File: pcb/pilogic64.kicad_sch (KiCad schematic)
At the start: 4 parts, among them U2 Pico

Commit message: More pcb!
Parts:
- added D1: D_Schottky, Diode_THT:D_DO-41_SOD81_P10.16mm_Horizontal, symbol Device:D_Schottky
- added SW1, SW2: RotaryEncoder_Switch, Rotary_Encoder:RotaryEncoder_Alps_EC11E-Switch_Vertical_H20mm, symbol Device:RotaryEncoder_Switch
- added b18650: ~, Battery:BatteryHolder_MPD_BH-18650-PC2, symbol LibrarySym:18650
- SD_SPI1: renamed from SD_SPI; footprint (none) -> Connector_PinHeader_2.54mm:PinHeader_1x06_P2.54mm_Vertical
- U2: footprint RPi_Pico:RPi_Pico_SMD_TH -> Library:RPi_Pico_SMD_TH
- renumbered MT3608_module_SMT to MT3608_module_SMT1
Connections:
- net at TP4056-18650.3 (OUT+): now also MT3608_module_SMT1.1 (VIN+)
- net at TP4056-18650.4 (OUT-): now also MT3608_module_SMT1.2 (VIN-)
- net at TP4056-18650.5 (B+): now also b18650.1 (+)
- net at TP4056-18650.6 (B-): now also b18650.2 (-)
- net GND: now reaches MT3608_module_SMT1.3 (VOUT-)
- net GND: now also SD_SPI1.6 (GND), U2.13 (GND), U2.18 (GND), U2.23 (GND), U2.28 (GND), U2.3 (GND), U2.38 (GND), U2.8 (GND), SW1.C, SW1.S2, SW2.C, SW2.S2
- net +5V: now reaches MT3608_module_SMT1.4 (VOUT+)
- net +5V: now also D1.2 (A)
- net +3.3V: now reaches SD_SPI1.1 (3.3V)
- net +3.3V: now also U2.36 (3V3), SW1.A, SW2.A
- net at SD_SPI1.2 (cs): now also U2.2 (GPIO1)
- net at SD_SPI1.3 (MOSI): now also U2.5 (GPIO3)
- net at SD_SPI1.4 (CLK): now also U2.4 (GPIO2)
- net at SD_SPI1.5 (MISO): now also U2.6 (GPIO4)
- net at U2.10 (GPIO7): now also SW2.S1
- net at U2.11 (GPIO8): now also SW1.B
- net at U2.12 (GPIO9): now also SW1.S1
- net at U2.39 (VSYS): now also D1.1 (K)
- net at U2.9 (GPIO6): now also SW2.B
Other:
- moved on the sheet: MT3608_module_SMT1, SD_SPI1, U2

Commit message: Finished cicuit, and I think also finished pcb
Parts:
- added U1: ~, Connector_PinHeader_2.54mm:PinHeader_1x04_P2.54mm_Vertical, symbol LibrarySym:I2C_OLED
- added U3: pam8403, Library:pam8403, symbol LibrarySym:pam8403
- b18650: footprint Battery:BatteryHolder_MPD_BH-18650-PC2 -> Library:18650-PC4
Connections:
- net +3.3V: now also U1.2 (VCC)
- net +5V: now also U3.4 (vin)
- net GND: now also U1.1 (GND), U3.2 (T), U3.5 (gnd)
- net at TP4056-18650.5 (B+): now also b18650.+1 (+), b18650.+2 (+); no longer b18650.1 (+)
- net at TP4056-18650.6 (B-): now also b18650.-1 (-), b18650.-2 (-); no longer b18650.2 (-)
- net at U2.14 (GPIO10): now also U1.4 (SDA)
- net at U2.15 (GPIO11): now also U1.3 (SCL)
- net at U2.19 (GPIO14): now also U3.3 (R)
- net at U2.20 (GPIO15): now also U3.1 (L)
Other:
- moved on the sheet: D1, MT3608_module_SMT1, SD_SPI1, TP4056-18650

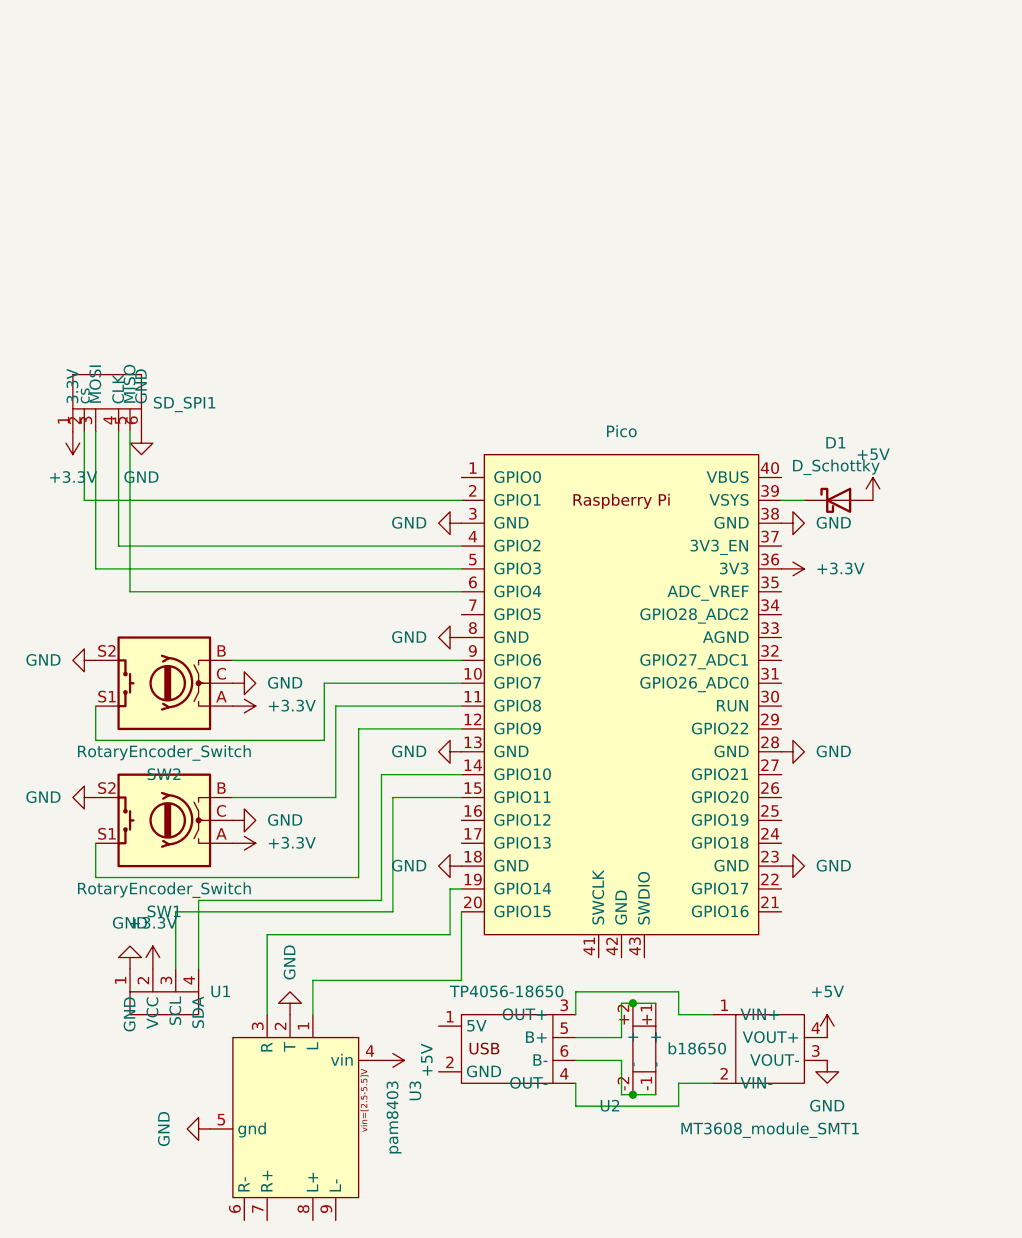
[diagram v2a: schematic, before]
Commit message: Add new symbols for components and remove lock files; implement main functionality for game selection on microcontroller
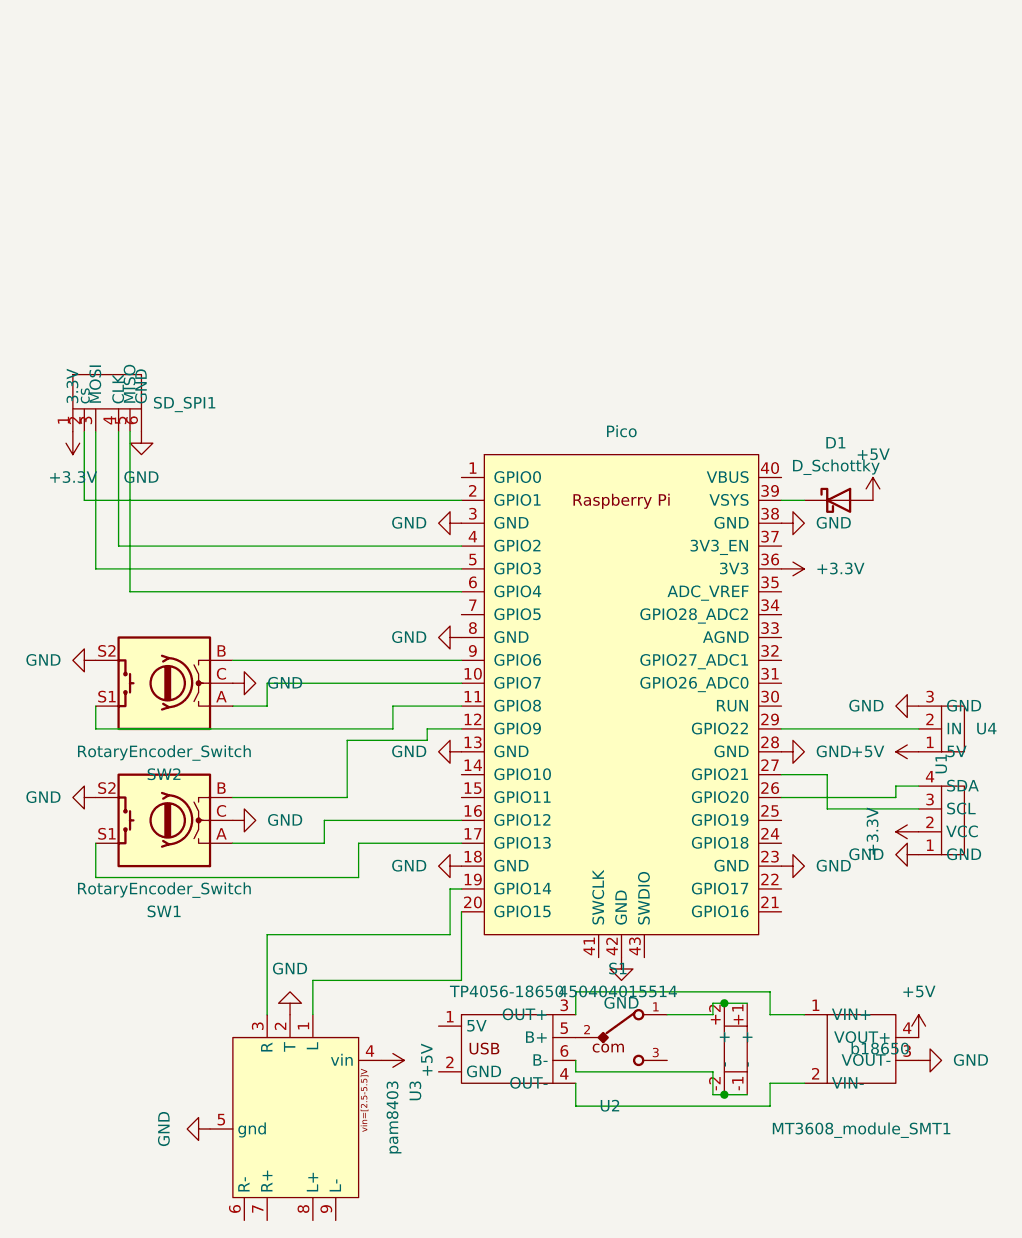
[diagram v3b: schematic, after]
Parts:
- added S1: 450404015514, Library:450404015514, symbol LibrarySym:450404015514
- added U4: ~, Library:8x8 MAtrix, symbol LibrarySym:8x8_matrix
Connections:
- net +3.3V: no longer SW1.A, SW2.A
- net +5V: now also U4.1 (5V)
- net GND: now also U2.42 (GND), U4.3 (GND)
- net at b18650.+1 (+), b18650.+2 (+): now also S1.1; no longer TP4056-18650.5 (B+)
- net at U2.10 (GPIO7): now also SW2.A; no longer SW2.S1
- net at U1.3 (SCL): now also U2.27 (GPIO21); no longer U2.15 (GPIO11)
- net at U1.4 (SDA): now also U2.26 (GPIO20); no longer U2.14 (GPIO10)
- net at U2.11 (GPIO8): now also SW2.S1; no longer SW1.B
- net at U2.12 (GPIO9): now also SW1.B; no longer SW1.S1
- net at U2.16 (GPIO12): now also SW1.A
- net at U2.17 (GPIO13): now also SW1.S1
- net at U2.29 (GPIO22): now also U4.2 (IN)
- new net: S1.2, TP4056-18650.5 (B+)
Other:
- moved on the sheet: MT3608_module_SMT1, U1, b18650
